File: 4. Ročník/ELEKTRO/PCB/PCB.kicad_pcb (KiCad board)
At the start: 2 copper layers, 60 x 65 mm, 9 parts, among them J1 Conn_01x04, J11 Jetson Pinout, J12 Screw_Terminal_01x02, J13 Screw_Terminal_01x02, J14 Screw_Terminal_01x02, J15 Napajeni BTS_R, J16 Napajeni BTS_L, J3 Conn_01x08, J8 Conn_01x08

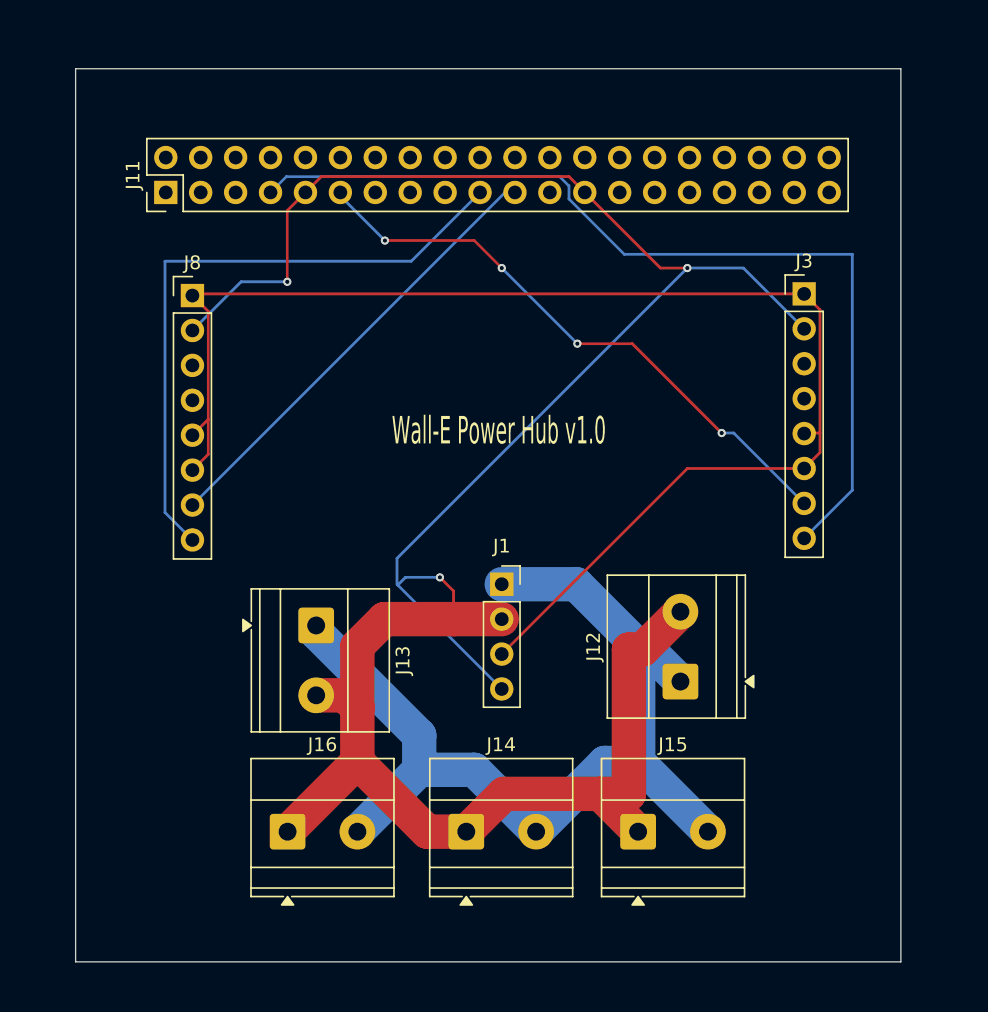
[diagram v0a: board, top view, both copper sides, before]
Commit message: PCB v1.0 fixes: 0.4/0.8mm routing, GND plane pour, silkscreen updates
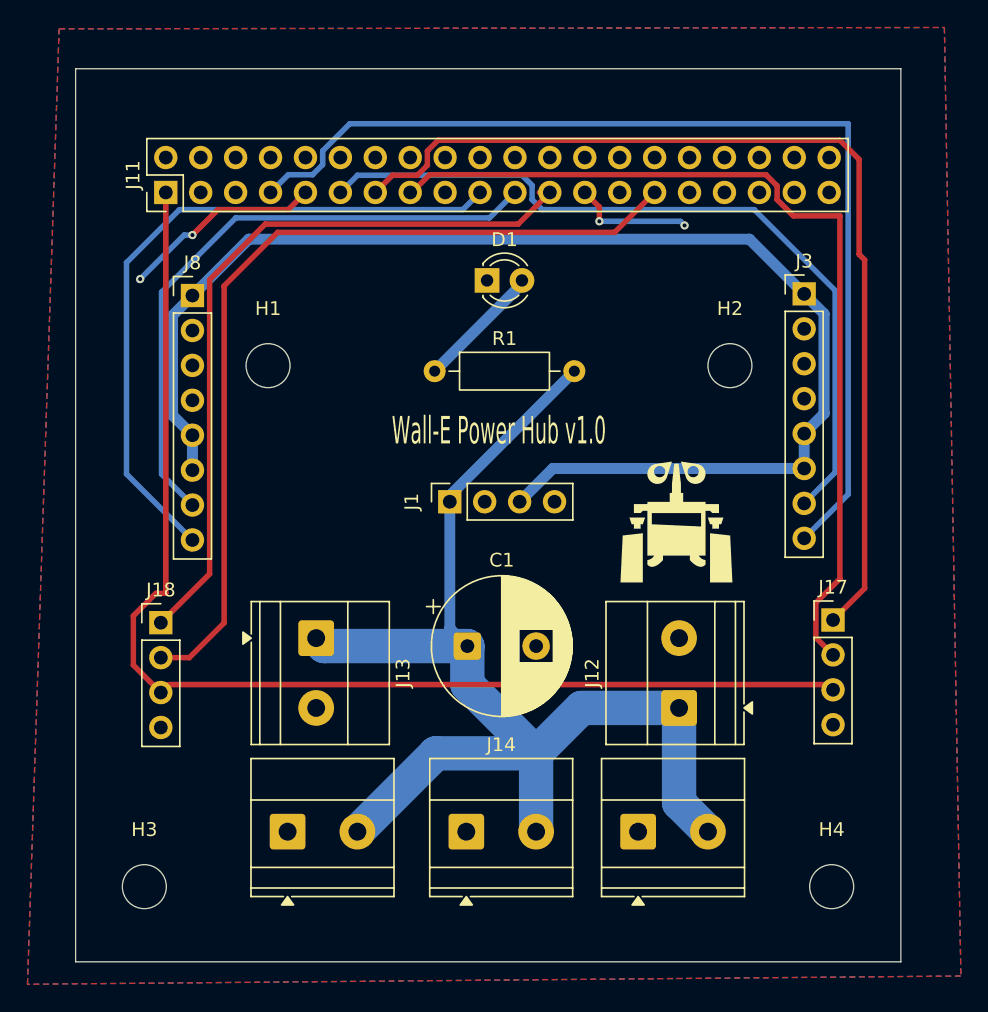
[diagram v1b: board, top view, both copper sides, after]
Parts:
- added C1: 1000uF / 35V, Capacitor_THT:CP_Radial_D10.0mm_P5.00mm, F.Cu at (113.5, 88.5)
- added D1: LED, LED_THT:LED_D3.0mm, F.Cu at (114.9, 61.9)
- added H1: MountingHole, MountingHole:MountingHole_3.2mm_M3, F.Cu at (99.0, 68.1)
- added H2: MountingHole, MountingHole:MountingHole_3.2mm_M3, F.Cu at (132.6, 68.1)
- added H3: MountingHole, MountingHole:MountingHole_3.2mm_M3, F.Cu at (90.0, 106.0)
- added H4: MountingHole, MountingHole:MountingHole_3.2mm_M3, F.Cu at (140.0, 106.0)
- added J17: Conn_01x04, Connector_PinHeader_2.54mm:PinHeader_1x04_P2.54mm_Vertical, F.Cu at (140.1, 86.6)
- added J18: Conn_01x04, Connector_PinHeader_2.54mm:PinHeader_1x04_P2.54mm_Vertical, F.Cu at (91.2, 86.8)
- added R1: 1k, Resistor_THT:R_Axial_DIN0207_L6.3mm_D2.5mm_P10.16mm_Horizontal, F.Cu at (111.1, 68.5)
- moved J1 7.09 mm to (112.2, 78.0), turned to 90 degrees
- moved J12 1.92 mm to (128.9, 93.0)
- moved J13 0.92 mm to (102.5, 87.9)
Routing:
- net GND: track 178.6 -> 23.6 mm, vias 3 -> 4
- net +3V3: track 0.00 -> 87.9 mm
- net /MOTOR_R_ENK_A: track 0.00 -> 72.6 mm
- net /MOTOR_R_ENK_B: track 0.00 -> 66.8 mm
- net /MOTOR_L_ENK_B: track 0.00 -> 64.3 mm
- net /MOTOR_L_ENK_A: track 0.00 -> 54.6 mm
- net +12V: track 71.4 -> 88.1 mm
- net /R_RPWM: track 43.3 -> 57.0 mm, vias 4 -> 0
- net /L_RPWM: track 32.9 -> 45.1 mm
- net Net-(D1-A): track 0.00 -> 9.23 mm
- net /R_LPWM: track 67.8 -> 76.2 mm
- net +5V: track 102.6 -> 97.4 mm
- net /L_LPWM: track 46.1 -> 50.0 mm
- added copper zone on B.Cu, net GND
- added copper zone on F.Cu, net GND
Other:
- board text added: "Made from tears and suffering"
